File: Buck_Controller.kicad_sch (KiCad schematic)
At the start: 15 parts, among them U1 LM25085MM, U2 LM25085MM

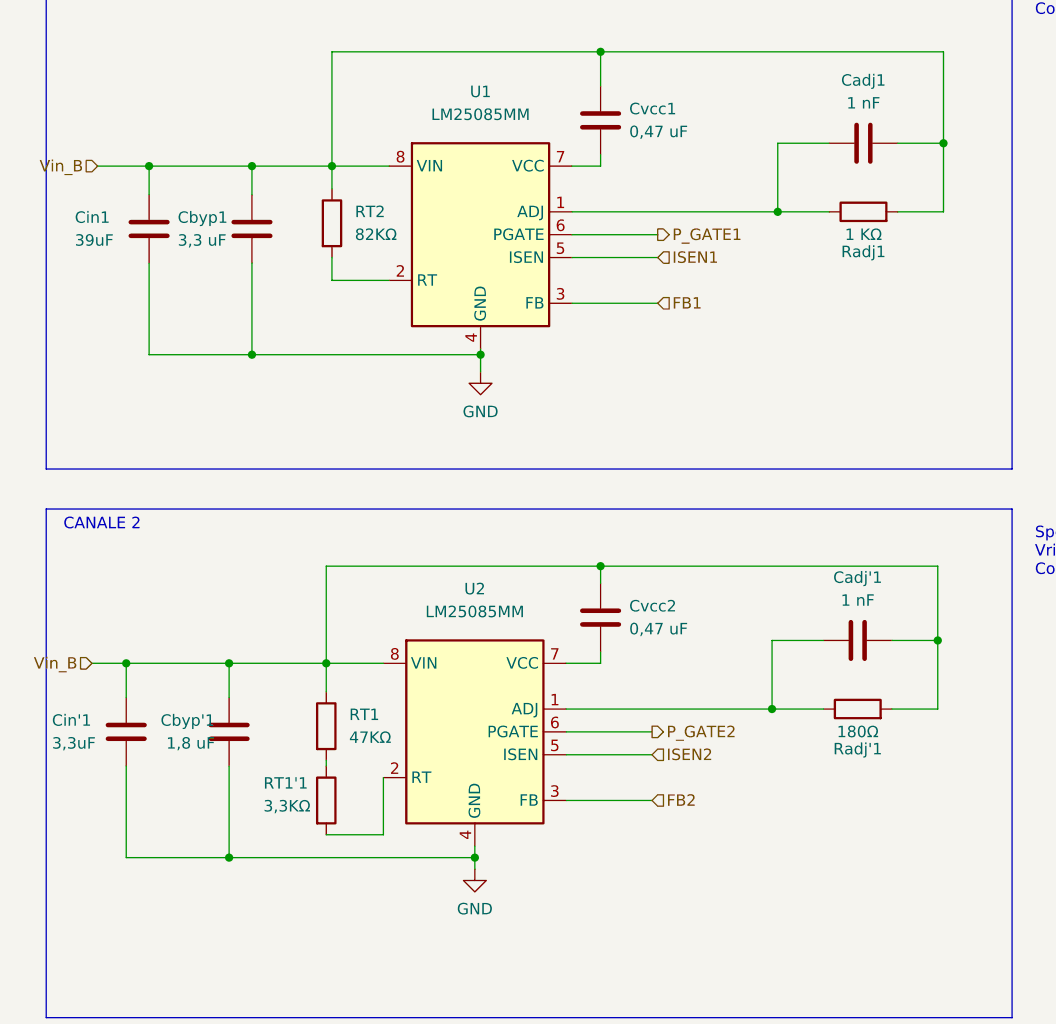
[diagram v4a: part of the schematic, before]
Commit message: modificalo lo schematic e rifatto in parte il design PCB
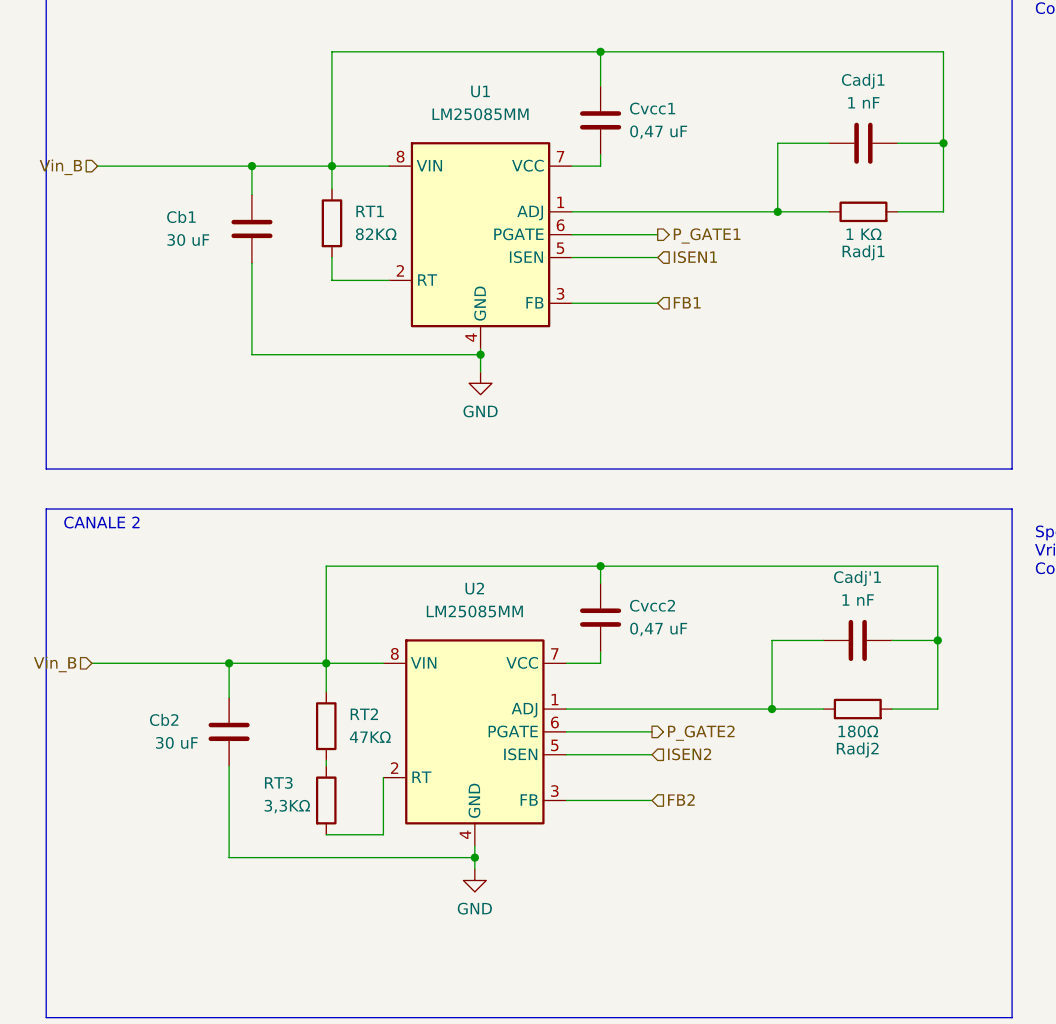
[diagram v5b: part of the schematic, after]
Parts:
- removed Cin'1: 3,3uF, Capacitor_SMD:C_0603_1608Metric, symbol Device:C
- removed Cin1: 39uF, Capacitor_SMD:C_0603_1608Metric, symbol Device:C
- Cb1: renamed from Cbyp1; value 3,3 uF -> 30 uF
- Cb2: renamed from Cbyp'1; value 1,8 uF -> 30 uF
- renumbered RT2 to RT1, RT1 to RT2, RT1'1 to RT3, Radj'1 to Radj2
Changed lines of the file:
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@@
   (junction (at 50.165 45.085) (diameter 0) (color 0 0 0 0)
   )
-  (junction (at 50.165 66.04) (diameter 0) (color 0 0 0 0)
-  )
-  (junction (at 38.735 45.085) (diameter 0) (color 0 0 0 0)
-  )
-  (junction (at 36.195 100.33) (diameter 0) (color 0 0 0 0)
-  )
   (junction (at 108.585 50.165) (diameter 0) (color 0 0 0 0)
   )
@@
   (junction (at 74.93 121.92) (diameter 0) (color 0 0 0 0)
   )
-  (junction (at 47.625 121.92) (diameter 0) (color 0 0 0 0)
-  )
   (junction (at 126.365 97.79) (diameter 0) (color 0 0 0 0)
   )
@@
     (stroke (width 0) (type default) (color 0 0 0 0))
   )
-  (wire (pts (xy 38.735 45.085) (xy 38.735 48.26))
-    (stroke (width 0) (type default) (color 0 0 0 0))
-  )
   (wire (pts (xy 88.9 89.535) (xy 88.9 91.44))
     (stroke (width 0) (type default) (color 0 0 0 0))
@@
     (stroke (width 0) (type default) (color 0 0 0 0))
   )
-  (wire (pts (xy 36.195 111.76) (xy 36.195 121.92))
-    (stroke (width 0) (type default) (color 0 0 0 0))
-  )
-  (wire (pts (xy 38.735 66.04) (xy 50.165 66.04))
-    (stroke (width 0) (type default) (color 0 0 0 0))
-  )
   (wire (pts (xy 126.365 89.535) (xy 126.365 97.79))
     (stroke (width 0) (type default) (color 0 0 0 0))
@@
     (stroke (width 0) (type default) (color 0 0 0 0))
   )
-  (wire (pts (xy 33.02 45.085) (xy 38.735 45.085))
-    (stroke (width 0) (type default) (color 0 0 0 0))
-  )
   (wire (pts (xy 59.055 32.385) (xy 59.055 45.085))
     (stroke (width 0) (type default) (color 0 0 0 0))
@@
     (stroke (width 0) (type default) (color 0 0 0 0))
   )
-  (wire (pts (xy 38.735 55.88) (xy 38.735 66.04))
-    (stroke (width 0) (type default) (color 0 0 0 0))
-  )
-  (wire (pts (xy 32.385 100.33) (xy 36.195 100.33))
+  (wire (pts (xy 32.385 100.33) (xy 47.625 100.33))
     (stroke (width 0) (type default) (color 0 0 0 0))
   )
@@
     (stroke (width 0) (type default) (color 0 0 0 0))
   )
-  (wire (pts (xy 36.195 100.33) (xy 47.625 100.33))
-    (stroke (width 0) (type default) (color 0 0 0 0))
-  )
   (wire (pts (xy 121.285 97.79) (xy 126.365 97.79))
     (stroke (width 0) (type default) (color 0 0 0 0))
   )
-  (wire (pts (xy 36.195 100.33) (xy 36.195 104.14))
-    (stroke (width 0) (type default) (color 0 0 0 0))
-  )
   (wire (pts (xy 127 32.385) (xy 88.9 32.385))
     (stroke (width 0) (type default) (color 0 0 0 0))
@@
     (stroke (width 0) (type default) (color 0 0 0 0))
   )
-  (wire (pts (xy 38.735 45.085) (xy 50.165 45.085))
+  (wire (pts (xy 33.02 45.085) (xy 50.165 45.085))
     (stroke (width 0) (type default) (color 0 0 0 0))
   )
@@
   )
   (wire (pts (xy 85.09 105.41) (xy 107.95 105.41))
-    (stroke (width 0) (type default) (color 0 0 0 0))
-  )
-  (wire (pts (xy 36.195 121.92) (xy 47.625 121.92))
     (stroke (width 0) (type default) (color 0 0 0 0))
   )
@@
   (symbol (lib_id "Device:R") (at 58.42 107.315 0) (unit 1)
     (in_bom yes) (on_board yes) (fields_autoplaced)
-    (property "Reference" "RT1" (id 0) (at 60.96 106.0449 0)
+    (property "Reference" "RT2" (id 0) (at 60.96 106.0449 0)
       (effects (font (size 1.27 1.27)) (justify left))
     )
@@
     (pin "2")
   )
-  (symbol (lib_id "Device:C") (at 36.195 107.95 0) (unit 1)
-    (in_bom yes) (on_board yes)
-    (property "Reference" "Cin'1" (id 0) (at 27.94 106.68 0)
-      (effects (font (size 1.27 1.27)) (justify left))
-    )
-    (property "Value" "3,3uF" (id 1) (at 27.94 109.22 0)
-      (effects (font (size 1.27 1.27)) (justify left))
-    )
-    (property "Footprint" "Capacitor_SMD:C_0603_1608Metric" (id 2) (at 37.1602 111.76 0)
-      (effects (font (size 1.27 1.27)) hide)
-    )
-    (property "Datasheet" "~" (id 3) (at 36.195 107.95 0)
-      (effects (font (size 1.27 1.27)) hide)
-    )
-    (pin "1")
-    (pin "2")
-  )
   (symbol (lib_id "Device:R") (at 59.055 51.435 0) (unit 1)
     (in_bom yes) (on_board yes) (fields_autoplaced)
-    (property "Reference" "RT2" (id 0) (at 61.595 50.1649 0)
+    (property "Reference" "RT1" (id 0) (at 61.595 50.1649 0)
       (effects (font (size 1.27 1.27)) (justify left))
     )
@@
   (symbol (lib_id "Device:R") (at 117.475 105.41 90) (unit 1)
     (in_bom yes) (on_board yes)
-    (property "Reference" "Radj'1" (id 0) (at 117.475 109.855 90))
+    (property "Reference" "Radj2" (id 0) (at 117.475 109.855 90))
     (property "Value" "180Ω" (id 1) (at 117.475 107.95 90))
     (property "Footprint" "Resistor_SMD:R_0402_1005Metric" (id 2) (at 117.475 107.188 90)
@@
     )
     (property "Datasheet" "~" (id 3) (at 117.475 105.41 0)
-      (effects (font (size 1.27 1.27)) hide)
-    )
-    (pin "1")
-    (pin "2")
-  )
-  (symbol (lib_id "Device:C") (at 38.735 52.07 0) (unit 1)
-    (in_bom yes) (on_board yes)
-    (property "Reference" "Cin1" (id 0) (at 30.48 50.8 0)
-      (effects (font (size 1.27 1.27)) (justify left))
-    )
-    (property "Value" "39uF" (id 1) (at 30.48 53.34 0)
-      (effects (font (size 1.27 1.27)) (justify left))
-    )
-    (property "Footprint" "Capacitor_SMD:C_0603_1608Metric" (id 2) (at 39.7002 55.88 0)
-      (effects (font (size 1.27 1.27)) hide)
-    )
-    (property "Datasheet" "~" (id 3) (at 38.735 52.07 0)
       (effects (font (size 1.27 1.27)) hide)
     )
@@
   (symbol (lib_id "Device:R") (at 58.42 115.57 0) (unit 1)
     (in_bom yes) (on_board yes)
-    (property "Reference" "RT1'1" (id 0) (at 51.435 113.665 0)
+    (property "Reference" "RT3" (id 0) (at 51.435 113.665 0)
       (effects (font (size 1.27 1.27)) (justify left))
     )
@@
   (symbol (lib_id "Device:C") (at 50.165 52.07 0) (unit 1)
     (in_bom yes) (on_board yes)
-    (property "Reference" "Cbyp1" (id 0) (at 41.91 50.8 0)
-      (effects (font (size 1.27 1.27)) (justify left))
-    )
-    (property "Value" "3,3 uF" (id 1) (at 41.91 53.34 0)
+    (property "Reference" "Cb1" (id 0) (at 40.64 50.8 0)
+      (effects (font (size 1.27 1.27)) (justify left))
+    )
+    (property "Value" "30 uF" (id 1) (at 40.64 53.34 0)
       (effects (font (size 1.27 1.27)) (justify left))
     )
@@
   (symbol (lib_id "Device:C") (at 47.625 107.95 0) (unit 1)
     (in_bom yes) (on_board yes)
-    (property "Reference" "Cbyp'1" (id 0) (at 40.005 106.68 0)
-      (effects (font (size 1.27 1.27)) (justify left))
-    )
-    (property "Value" "1,8 uF" (id 1) (at 40.64 109.22 0)
-      (effects (font (size 1.27 1.27)) (justify left))
-    )
+    (property "Reference" "Cb2" (id 0) (at 38.735 106.68 0)
+      (effects (font (size 1.27 1.27)) (justify left))
+    )
+    (property "Value" "30 uF" (id 1) (at 39.37 109.22 0)
+      (effects (font (size 1.27 1.27)) (justify left))
+    )
